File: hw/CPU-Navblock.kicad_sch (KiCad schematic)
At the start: 33 parts, among them J4001 Conn_01x08, J4002 Conn_01x03, J4003 Conn_01x02, J4004 Conn_01x02, J4005 Conn_01x02, J4006 Conn_01x02, P4000 Current-Probe, U4000 STM32F401XX-LQFP64, U4001 TLV62150A, Y4000 MCSJK-7I-8.00-18-30-60-B-30

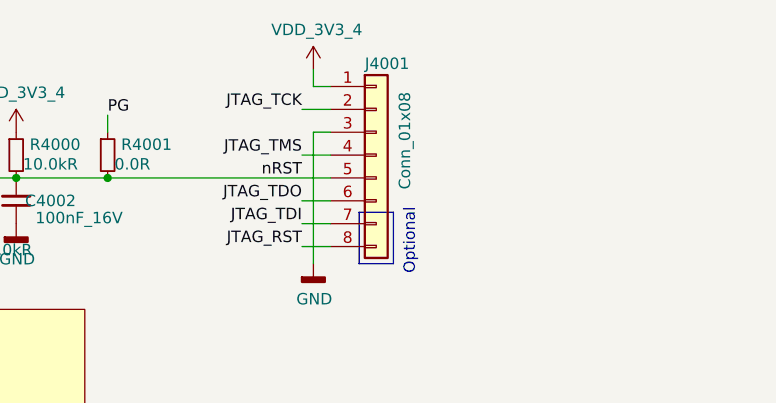
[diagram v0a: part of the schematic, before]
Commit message: Replace JTAG connectors with angled ones one back side.
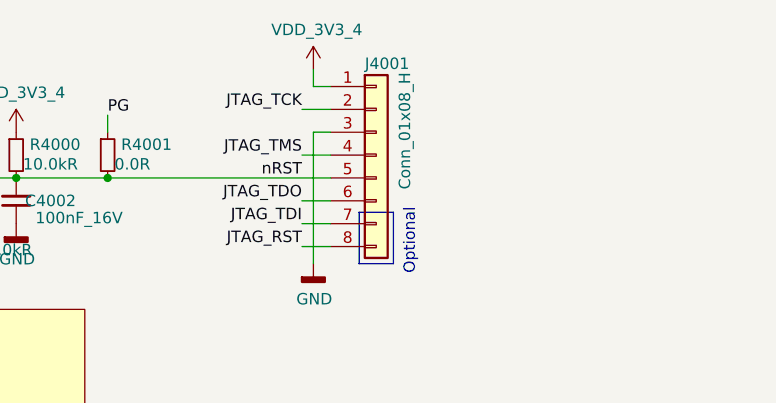
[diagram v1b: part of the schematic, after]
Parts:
- J4001: value Conn_01x08 -> Conn_01x08_H; footprint Keyboard:Pin_Header_Straight_1x08_Pitch2.54mm -> Keyboard:Pin_Header_Horizontal_1x08_Pitch2.54mm; symbol Keyboard:Conn_01x08 -> Keyboard:Conn_01x08_H; farnell# 1593416 -> 1593431
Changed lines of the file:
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@@
     )
   )
-  (symbol (lib_id "Keyboard:Conn_01x08") (at 226.695 33.655 0) (unit 1)
+  (symbol (lib_id "Keyboard:Conn_01x08_H") (at 226.695 33.655 0) (unit 1)
     (in_bom yes) (on_board yes) (dnp no)
     (property "Reference" "J4001" (at 225.425 23.495 0)
       (effects (font (size 1.27 1.27)) (justify left))
     )
-    (property "Value" "Conn_01x08" (at 229.87 37.465 90)
+    (property "Value" "Conn_01x08_H" (at 229.87 37.465 90)
       (effects (font (size 1.27 1.27)) (justify left))
     )
-    (property "Footprint" "Keyboard:Pin_Header_Straight_1x08_Pitch2.54mm" (at 224.155 26.035 0)
+    (property "Footprint" "Keyboard:Pin_Header_Horizontal_1x08_Pitch2.54mm" (at 224.155 26.035 0)
       (effects (font (size 1.27 1.27)) hide)
     )
-    (property "Datasheet" "Multicomp  2211S-08G" (at 226.695 23.495 0)
+    (property "Datasheet" "Multicomp  34753" (at 226.695 23.495 0)
       (effects (font (size 1.27 1.27)) hide)
     )
-    (property "farnell#" "1593416" (at 226.695 20.955 0)
+    (property "farnell#" "1593431" (at 226.695 20.955 0)
       (effects (font (size 1.524 1.524)) hide)
     )
